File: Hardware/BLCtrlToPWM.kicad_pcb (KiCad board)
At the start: 2 copper layers, 62 x 50 mm, 34 parts, among them IC1 ATMEGA2560-A, Y1 16MHz

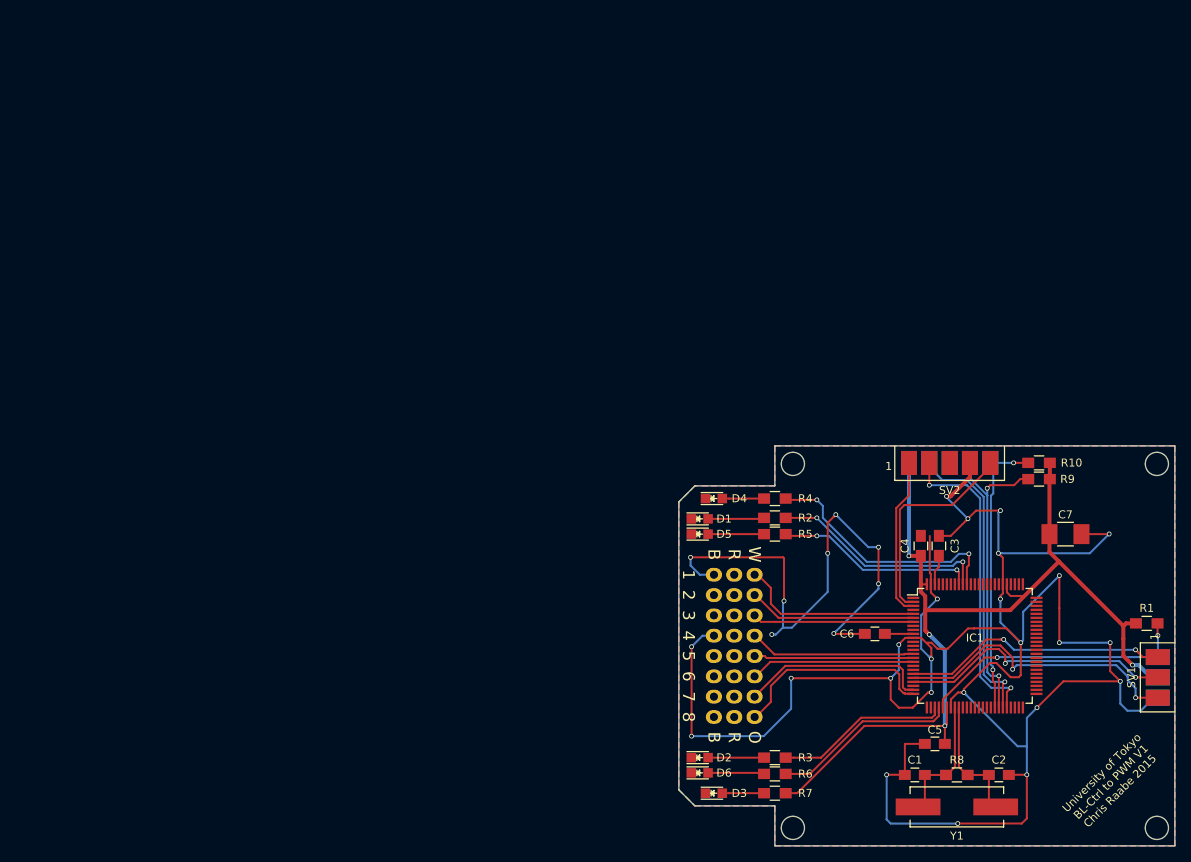
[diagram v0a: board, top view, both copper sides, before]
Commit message: Updated board layout with new components, but they are yet to be placed and traces need to be added
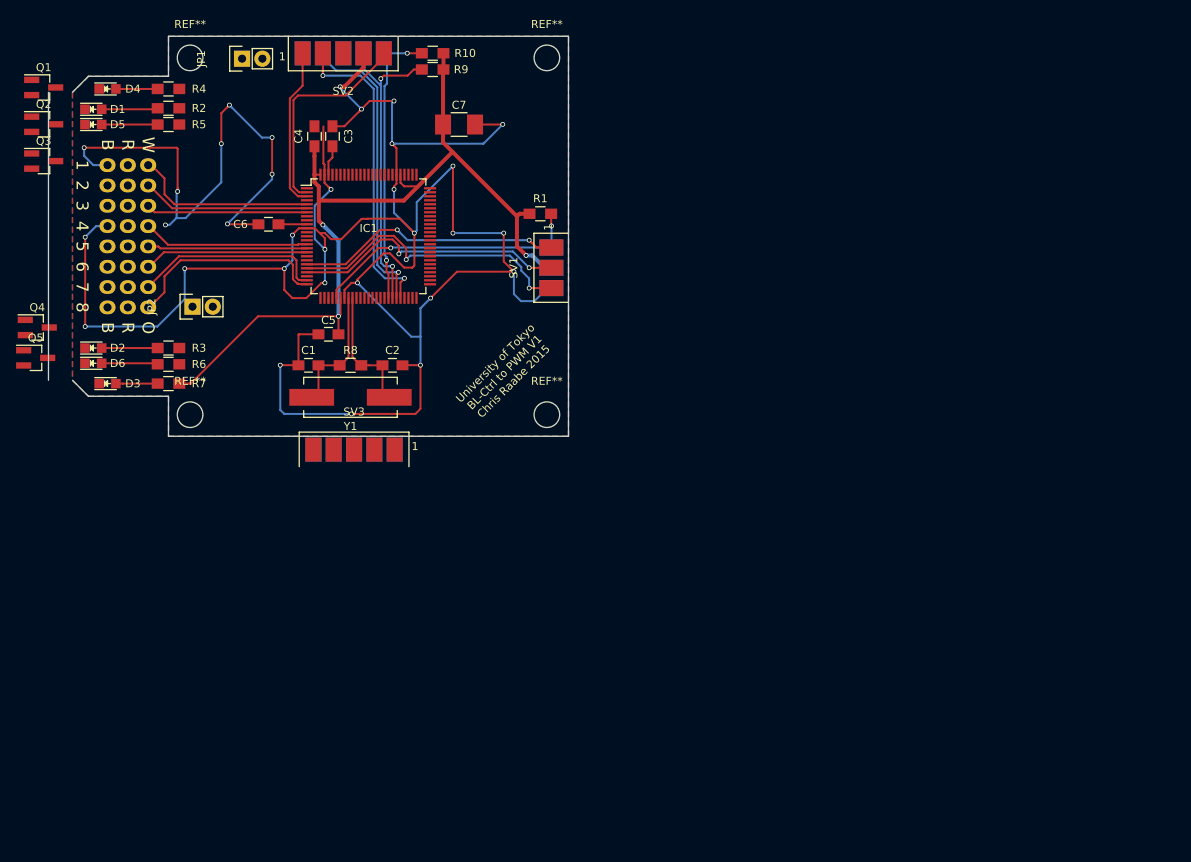
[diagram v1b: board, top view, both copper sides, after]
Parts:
- removed the REF** at (53.0, 28.4)
- removed the REF** at (98.5, 28.4)
- removed the REF** at (98.5, 74.0)
- removed the REF** at (53.0, 74.0)
- added JP1: Jumper_NO_Small, Pin_Headers:Pin_Header_Straight_1x02, F.Cu at (-15.8, -22.2)
- added JP2: Jumper_NO_Small, Pin_Headers:Pin_Header_Straight_1x02, F.Cu at (-22.0, 8.80)
- added Q1: Q_NMOS_GSD, TO_SOT_Packages_SMD:SOT-23_Handsoldering, F.Cu at (-40.6, -18.6)
- added Q2: Q_NMOS_GSD, TO_SOT_Packages_SMD:SOT-23_Handsoldering, F.Cu at (-40.6, -14.0)
- added Q3: Q_NMOS_GSD, TO_SOT_Packages_SMD:SOT-23_Handsoldering, F.Cu at (-40.6, -9.40)
- added Q4: Q_NMOS_GSD, TO_SOT_Packages_SMD:SOT-23_Handsoldering, F.Cu at (-41.4, 11.4)
- added Q5: Q_NMOS_GSD, TO_SOT_Packages_SMD:SOT-23_Handsoldering, F.Cu at (-41.6, 15.2)
- added REF**: MountingHole_3.2mm_M3, Mounting_Holes:MountingHole_3.2mm_M3, F.Cu at (-22.3, 22.3)
- added REF**: MountingHole_3.2mm_M3, Mounting_Holes:MountingHole_3.2mm_M3, F.Cu at (22.3, 22.3)
- added REF**: MountingHole_3.2mm_M3, Mounting_Holes:MountingHole_3.2mm_M3, F.Cu at (22.3, -22.3)
- added REF**: MountingHole_3.2mm_M3, Mounting_Holes:MountingHole_3.2mm_M3, F.Cu at (-22.3, -22.3)
- added SV3: MKDebug, Pin_Headers_Edge:Pin_Header_Edge_2x05, F.Cu at (-1.80, 28.8)
- R2, R3, R4, R5, R6: value 1k -> 470
- moved C1 91.5 mm to (-7.50, 16.1)
- moved C2 91.5 mm to (3.00, 16.1)
- moved C3 91.5 mm to (-4.50, -12.5)
- moved C4 91.5 mm to (-6.75, -12.5)
- moved C5 91.5 mm to (-5.00, 12.2)
- moved C6 91.5 mm to (-12.5, -1.50)
- moved D1 91.5 mm to (-34.4, -15.9)
- moved D2 91.5 mm to (-34.4, 14.0)
- moved D5 91.5 mm to (-34.4, -14.0)
- moved D6 91.5 mm to (-34.4, 15.9)
- moved GND1 91.5 mm to (-32.6, -8.89)
- moved IC1 91.5 mm to (0.00, 0.00)
- moved PWM1 91.5 mm to (-27.5, -8.89)
- moved PWR1 91.5 mm to (-30.1, -8.89)
- moved R1 91.5 mm to (21.5, -2.81)
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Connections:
- D1 pad 1: Earth -> Net-(D1-Pad1)
- D2 pad 1: Earth -> Net-(D2-Pad1)
- D4 pad 1: Earth -> Net-(D4-Pad1)
- D5 pad 1: Earth -> Net-(D5-Pad1)
- D6 pad 1: Earth -> Net-(D6-Pad1)
- IC1 pad 3: Net-(IC1-Pad3) -> (no net)
- IC1 pad 46: Net-(IC1-Pad46) -> (no net)
- IC1 pad 63: (no net) -> Net-(IC1-Pad63)
- IC1 pad 64: (no net) -> Net-(IC1-Pad64)
- PWR1 pad 1: (no net) -> Net-(JP2-Pad1)
- PWR1 pad 2: (no net) -> Net-(JP2-Pad1)
- PWR1 pad 3: (no net) -> Net-(JP2-Pad1)
- PWR1 pad 4: (no net) -> Net-(JP2-Pad1)
- PWR1 pad 5: (no net) -> Net-(JP2-Pad1)
- PWR1 pad 6: (no net) -> Net-(JP2-Pad1)
- PWR1 pad 7: (no net) -> Net-(JP2-Pad1)
- PWR1 pad 8: (no net) -> Net-(JP2-Pad1)
- R2 pad 1: /RX_LED -> +5V
- R3 pad 1: /BLUE1_LED -> +5V
- R4 pad 1: /GREEN_LED -> +5V
- R5 pad 1: /TX_LED -> +5V
- R6 pad 1: /BLUE2_LED -> +5V
- SV2 pad 1: Net-(IC1-Pad3) -> Net-(IC1-Pad45)
- SV2 pad 2: +5V -> Net-(JP1-Pad2)
- SV2 pad 3: Net-(IC1-Pad46) -> (no net)
- SV2 pad 4: Net-(IC1-Pad45) -> (no net)
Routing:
- net (no net): track 0.00 -> 39.2 mm, vias 0 -> 2
- net Net-(IC1-Pad46): track 39.2 -> 0.00 mm, vias 2 -> 0
- net /GREEN_LED: track 31.4 -> 0.00 mm, vias 2 -> 0
- net /RX_LED: track 27.6 -> 0.00 mm, vias 2 -> 0
- net /TX_LED: track 25.2 -> 0.00 mm, vias 2 -> 0
- net /BLUE2_LED: track 23.2 -> 0.00 mm
- net /BLUE1_LED: track 22.4 -> 0.60 mm
- net Net-(IC1-Pad45): track 37.4 -> 57.5 mm
- net Net-(IC1-Pad3): track 20.1 -> 0.00 mm
- net +5V: track 125.7 -> 113.1 mm, vias 4 -> 3
- net Earth: track 350.0 -> 341.8 mm
- net Net-(JP2-Pad1): track 0.00 -> 8.24 mm
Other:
- board size 62 x 50 mm -> 65 x 50 mm

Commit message: Widened the gap between ESC headers
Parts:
- moved GND1 8.89 mm to (-32.6, 0.00)
- moved PWM1 8.89 mm to (-27.5, 0.00)
- moved PWR1 8.89 mm to (-30.1, 0.00)
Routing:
- net Net-(JP2-Pad1): track 8.24 -> 8.66 mm, vias 0 -> 1
- net Earth: track 341.8 -> 341.4 mm, vias 32 -> 31
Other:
- board text added: "University of Tokyo BL-Ctrl to PWM V2 Chris Raabe 2017"
- board text removed: "University of Tokyo BL-Ctrl to PWM V1 Chris Raabe 2015"

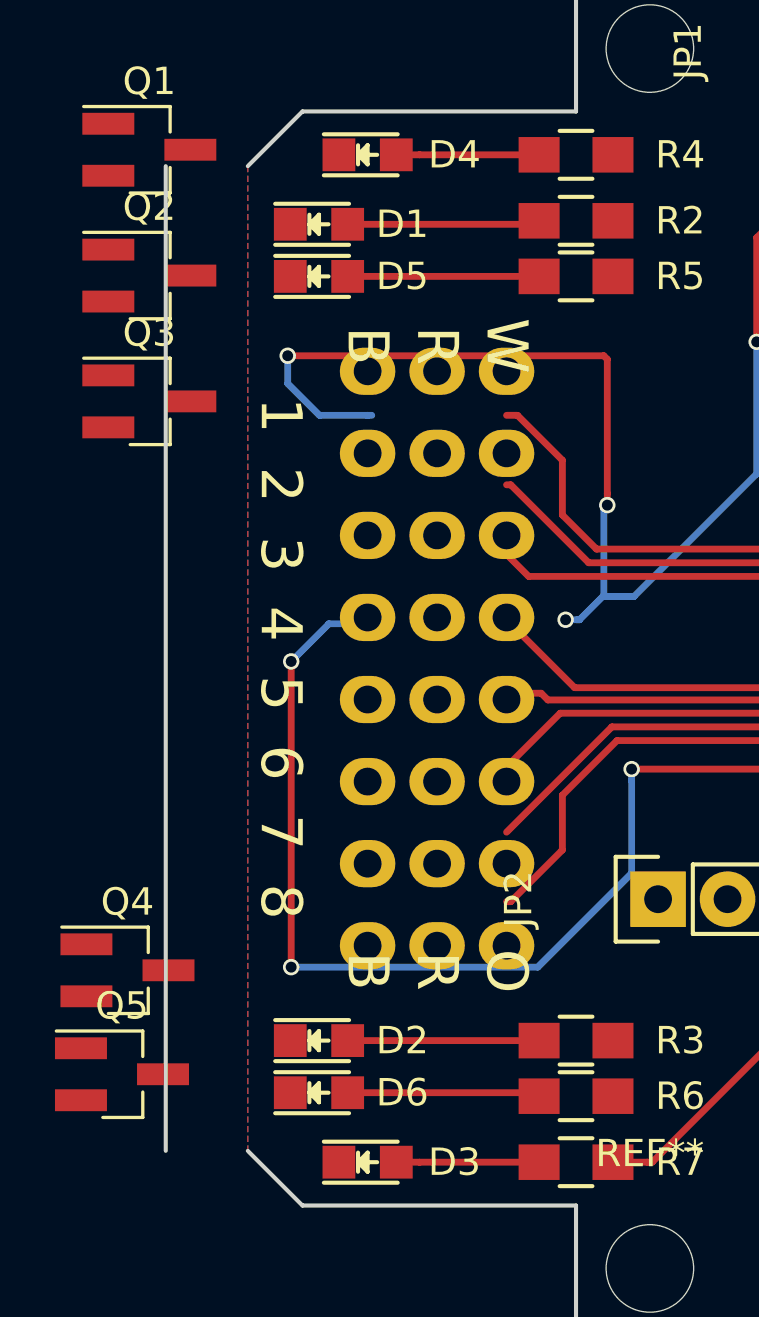
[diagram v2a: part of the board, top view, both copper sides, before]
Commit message: Small progress on board layout
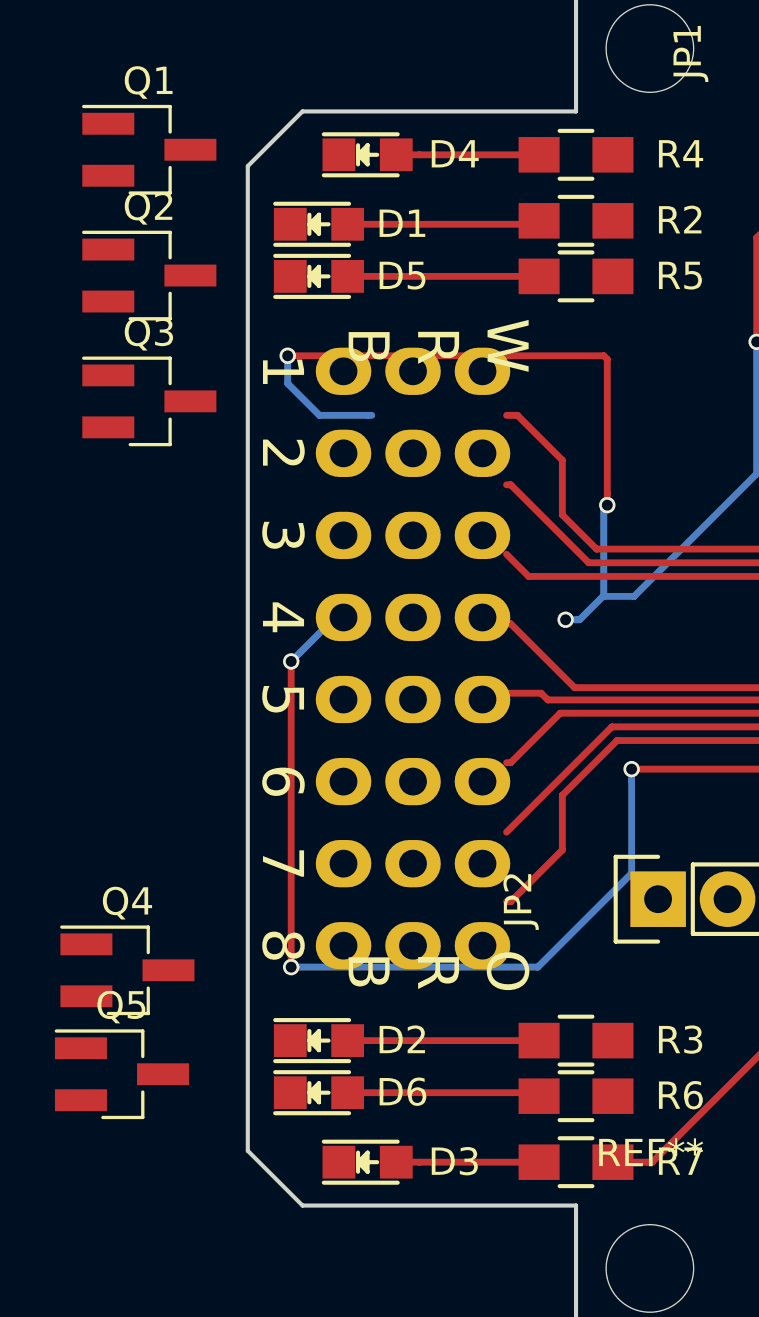
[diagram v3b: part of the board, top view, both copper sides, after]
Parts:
- moved GND1 0.88 mm to (-33.5, 0.00)
- moved PWM1 0.88 mm to (-28.4, 0.00)
- moved PWR1 0.88 mm to (-31.0, 0.00)
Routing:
- net Net-(JP2-Pad1): track 8.66 -> 8.24 mm, vias 1 -> 0
- net Earth: track 341.4 -> 341.8 mm, vias 31 -> 32
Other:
- board size 65 x 50 mm -> 62 x 50 mm
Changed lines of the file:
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@@
-  )
-  (module Mounting_Holes:MountingHole_3.2mm_M3 (layer F.Cu)
-    (at -22.3 22.3)
-    (descr "Mounting Hole 3.2mm, no annular, M3")
-    (tags "mounting hole 3.2mm no annular m3")
-    (fp_text reference REF** (at 0 -4.2) (layer F.SilkS)
-      (effects (font (size 1 1) (thickness 0.15)))
-    )
-    (fp_text value MountingHole_3.2mm_M3 (at 0 4.2) (layer F.Fab)
-      (effects (font (size 1 1) (thickness 0.15)))
-    )
-    (fp_circle (center 0 0) (end 3.2 0) (layer Cmts.User) (width 0.15))
-    (fp_circle (center 0 0) (end 3.45 0) (layer F.CrtYd) (width 0.05))
-    (pad 1 np_thru_hole circle (at 0 0) (size 3.2 3.2) (drill 3.2) (layers *.Cu *.Mask))
   )
   (module Mounting_Holes:MountingHole_3.2mm_M3 (layer F.Cu)
@@
   (module Mounting_Holes:MountingHole_3.2mm_M3 (layer F.Cu)
     (at 22.3 -22.3)
+    (descr "Mounting Hole 3.2mm, no annular, M3")
+    (tags "mounting hole 3.2mm no annular m3")
+    (fp_text reference REF** (at 0 -4.2) (layer F.SilkS)
+      (effects (font (size 1 1) (thickness 0.15)))
+    )
+    (fp_text value MountingHole_3.2mm_M3 (at 0 4.2) (layer F.Fab)
+      (effects (font (size 1 1) (thickness 0.15)))
+    )
+    (fp_circle (center 0 0) (end 3.2 0) (layer Cmts.User) (width 0.15))
+    (fp_circle (center 0 0) (end 3.45 0) (layer F.CrtYd) (width 0.05))
+    (pad 1 np_thru_hole circle (at 0 0) (size 3.2 3.2) (drill 3.2) (layers *.Cu *.Mask))
+  )
+  (module Mounting_Holes:MountingHole_3.2mm_M3 (layer F.Cu)
+    (at -22.3 22.3)
     (descr "Mounting Hole 3.2mm, no annular, M3")
     (tags "mounting hole 3.2mm no annular m3")
@@
   )
   (module Pin_Headers:Pin_Header_Straight_1x08 (layer F.Cu)
-    (at -32.62 0)
+    (at -33.5 0)
     (descr "Through hole pin header")
     (tags "pin header")
@@
   )
   (module Pin_Headers:Pin_Header_Straight_1x08 (layer F.Cu)
-    (at -30.08 0)
+    (at -30.96 0)
     (descr "Through hole pin header")
     (tags "pin header")
@@
   )
   (module Pin_Headers:Pin_Header_Straight_1x08 (layer F.Cu)
-    (at -27.54 0)
+    (at -28.42 0)
     (descr "Through hole pin header")
     (tags "pin header")
@@
   (gr_line (start -35 20) (end -25 20) (layer Edge.Cuts) (width 0.15))
   (gr_line (start -37 18) (end -35 20) (layer Edge.Cuts) (width 0.15))
-  (gr_line (start -40 -18) (end -40 18) (layer Edge.Cuts) (width 0.15))
+  (gr_line (start -37 -18) (end -37 18) (layer Edge.Cuts) (width 0.15))
   (gr_line (start -35 -20) (end -37 -18) (layer Edge.Cuts) (width 0.15))
   (gr_line (start -25 -20) (end -35 -20) (layer Edge.Cuts) (width 0.15))
   (gr_line (start -25 -25) (end -25 -20) (layer Edge.Cuts) (width 0.15))
   (gr_line (start 25 -25) (end -25 -25) (layer Edge.Cuts) (width 0.15))
-  (gr_text 8 (at -35.795 8.89 270) (layer F.SilkS)
+  (gr_text 8 (at -35.75 10.5 270) (layer F.SilkS)
     (effects (font (size 1.5 1.5) (thickness 0.3)))
   )
-  (gr_text 7 (at -35.795 6.35 270) (layer F.SilkS)
+  (gr_text 7 (at -35.75 7.5 270) (layer F.SilkS)
     (effects (font (size 1.5 1.5) (thickness 0.3)))
   )
-  (gr_text 6 (at -35.795 3.81 270) (layer F.SilkS)
+  (gr_text 6 (at -35.75 4.5 270) (layer F.SilkS)
     (effects (font (size 1.5 1.5) (thickness 0.3)))
   )
-  (gr_text 5 (at -35.795 1.27 270) (layer F.SilkS)
+  (gr_text 5 (at -35.75 1.5 270) (layer F.SilkS)
     (effects (font (size 1.5 1.5) (thickness 0.3)))
   )
-  (gr_text 4 (at -35.795 -1.27 270) (layer F.SilkS)
+  (gr_text 4 (at -35.75 -1.5 270) (layer F.SilkS)
     (effects (font (size 1.5 1.5) (thickness 0.3)))
   )
-  (gr_text 3 (at -35.795 -3.81 270) (layer F.SilkS)
+  (gr_text 3 (at -35.75 -4.5 270) (layer F.SilkS)
     (effects (font (size 1.5 1.5) (thickness 0.3)))
   )
-  (gr_text 2 (at -35.795 -6.35 270) (layer F.SilkS)
+  (gr_text 2 (at -35.75 -7.5 270) (layer F.SilkS)
     (effects (font (size 1.5 1.5) (thickness 0.3)))
   )
-  (gr_text 1 (at -35.795 -8.89 270) (layer F.SilkS)
+  (gr_text 1 (at -35.75 -10.5 270) (layer F.SilkS)
     (effects (font (size 1.5 1.5) (thickness 0.3)))
   )
@@
   (segment (start -10.522004 4.045) (end -10.522004 6.711996) (width 0.25) (layer F.Cu) (net 2))
   (via (at -10.522004 4.045) (size 0.6) (drill 0.4) (layers F.Cu B.Cu) (net 2))
+  (via (at -22.967994 4.045) (size 0.6) (drill 0.4) (layers F.Cu B.Cu) (net 2))
+  (segment (start -22.967994 4.469264) (end -22.967994 4.045) (width 0.25) (layer B.Cu) (net 2))
   (segment (start -2 7.7) (end -2 15.13) (width 0.25) (layer F.Cu) (net 3))
   (segment (start -2 15.13) (end -1 16.13) (width 0.25) (layer F.Cu) (net 3))
@@
   (segment (start -26.477 15.875) (end -26.35 16.002) (width 0.25) (layer F.Cu) (net 27))
   (segment (start -5 7.7) (end -5 8.3) (width 0.25) (layer F.Cu) (net 28))
-  (via (at -22.967994 4.045) (size 0.6) (drill 0.4) (layers F.Cu B.Cu) (net 41))
-  (segment (start -22.967994 4.469264) (end -22.967994 4.045) (width 0.25) (layer B.Cu) (net 41))
   (segment (start -22.967994 7.854994) (end -22.967994 4.469264) (width 0.25) (layer B.Cu) (net 41))
   (segment (start -26.397 11.284) (end -22.967994 7.854994) (width 0.25) (layer B.Cu) (net 41))
@@
       )
     )
-  )
-  (zone (net 0) (net_name "") (layer F.Cu) (hatch edge 0.508)
-    (connect_pads (clearance 0.508))
-    (min_thickness 0.254)
-    (keepout (tracks not_allowed) (vias not_allowed) (copperpour not_allowed))
-    (fill (arc_segments 16) (thermal_gap 0.508) (thermal_bridge_width 0.508))
-    (polygon
-      (pts
-        (xy -25 21) (xy -24 20) (xy -22 20) (xy -20 22) (xy -20 24)
-        (xy -21 25) (xy -25 25)
-      )
-    )
-  )
-  (zone (net 0) (net_name "") (layer F.Cu) (hatch edge 0.508)
-    (connect_pads (clearance 0.508))
-    (min_thickness 0.254)
-    (keepout (tracks not_allowed) (vias not_allowed) (copperpour not_allowed))
-    (fill (arc_segments 16) (thermal_gap 0.508) (thermal_bridge_width 0.508))
-    (polygon
-      (pts
-        (xy -25 -21) (xy -24 -20) (xy -22 -20) (xy -20 -22) (xy -20 -24)
-        (xy -21 -25) (xy -25 -25)
-      )
-    )
-  )
-  (zone (net 0) (net_name "") (layer F.Cu) (hatch edge 0.508)
-    (connect_pads (clearance 0.508))
-    (min_thickness 0.254)
-    (keepout (tracks not_allowed) (vias not_allowed) (copperpour not_allowed))
-    (fill (arc_segments 16) (thermal_gap 0.508) (thermal_bridge_width 0.508))
-    (polygon
-      (pts
-        (xy 21 -25) (xy 20 -24) (xy 20 -22) (xy 22 -20) (xy 24 -20)
-        (xy 25 -21) (xy 25 -25)
-      )
-    )
-  )
-  (zone (net 0) (net_name "") (layer B.Cu) (hatch edge 0.508)
-    (connect_pads (clearance 0.508))
-    (min_thickness 0.254)
-    (keepout (tracks not_allowed) (vias not_allowed) (copperpour not_allowed))
-    (fill (arc_segments 16) (thermal_gap 0.508) (thermal_bridge_width 0.508))
-    (polygon
-      (pts
-        (xy 21 -25) (xy 20 -24) (xy 20 -22) (xy 22 -20) (xy 24 -20)
-        (xy 25 -21) (xy 25 -25)
-      )
-    )
-  )
-  (zone (net 0) (net_name "") (layer B.Cu) (hatch edge 0.508)
-    (connect_pads (clearance 0.508))
-    (min_thickness 0.254)
-    (keepout (tracks not_allowed) (vias not_allowed) (copperpour not_allowed))
-    (fill (arc_segments 16) (thermal_gap 0.508) (thermal_bridge_width 0.508))
-    (polygon
-      (pts
-        (xy 25 21) (xy 24 20) (xy 22 20) (xy 20 22) (xy 20 24)
-        (xy 21 25) (xy 25 25)
-      )
-    )
-  )
-  (zone (net 0) (net_name "") (layer F.Cu) (hatch edge 0.508)
-    (connect_pads (clearance 0.508))
-    (min_thickness 0.254)
-    (keepout (tracks not_allowed) (vias not_allowed) (copperpour not_allowed))
-    (fill (arc_segments 16) (thermal_gap 0.508) (thermal_bridge_width 0.508))
-    (polygon
-      (pts
-        (xy 24 20) (xy 22 20) (xy 20 22) (xy 20 24) (xy 21 25)
-        (xy 25 25) (xy 25 21)
-      )
-    )
-  )
-  (zone (net 0) (net_name "") (layer B.Cu) (hatch edge 0.508)
-    (connect_pads (clearance 0.508))
-    (min_thickness 0.254)
-    (keepout (tracks not_allowed) (vias not_allowed) (copperpour not_allowed))
-    (fill (arc_segments 16) (thermal_gap 0.508) (thermal_bridge_width 0.508))
-    (polygon
-      (pts
-        (xy -21 25) (xy -20 24) (xy -20 22) (xy -22 20) (xy -24 20)
-        (xy -25 21) (xy -25 25)
-      )
-    )
-  )
-  (zone (net 0) (net_name "") (layer B.Cu) (hatch edge 0.508)
-    (connect_pads (clearance 0.508))
-    (min_thickness 0.254)
-    (keepout (tracks not_allowed) (vias not_allowed) (copperpour not_allowed))
-    (fill (arc_segments 16) (thermal_gap 0.508) (thermal_bridge_width 0.508))
-    (polygon
-      (pts
-        (xy -25 -21) (xy -24 -20) (xy -22 -20) (xy -20 -22) (xy -20 -24)
-        (xy -21 -25) (xy -25 -25)
-      )
-    )
